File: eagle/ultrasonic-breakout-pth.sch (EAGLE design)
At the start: 25 parts, among them Q1 16 MHz, U1 ATMEGA328P_PDIP

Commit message: improve board layout
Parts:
- C3: device SparkFun-Passives:CAPPTH1 -> SparkFun-Capacitors:CAPPTH
- Q1: device special:XTAL -> SparkFun-FreqCtrl:CRYSTALHC49UV
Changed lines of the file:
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@@
 <?xml version="1.0" encoding="utf-8"?>
 <!DOCTYPE eagle SYSTEM "eagle.dtd">
-<eagle version="7.5.0">
+<eagle version="7.1.0">
 <drawing>
 <settings>
@@
 <parts>
 <part name="U1" library="SparkFun-DigitalIC" deviceset="ATMEGA328P_PDIP" device=""/>
-<part name="Q1" library="special" deviceset="XTAL" device="" value="16 MHz"/>
+<part name="Q1" library="SparkFun-FreqCtrl" deviceset="CRYSTAL" device="HC49UV" value="16 MHz"/>
 <part name="C1" library="SparkFun-Passives" deviceset="CAP" device="PTH" value="2.2pF"/>
 <part name="C2" library="SparkFun-Passives" deviceset="CAP" device="PTH" value="2.2pF"/>
@@
 <part name="HCSR04-8" library="SparkFun-Connectors" deviceset="M04" device="PTH"/>
 <part name="R8" library="SparkFun-Passives" deviceset="RESISTOR" device="PTH-1/4W" value="2.2k"/>
-<part name="C3" library="SparkFun-Passives" deviceset="CAP" device="PTH1" value="0.1uF"/>
+<part name="C3" library="SparkFun-Capacitors" deviceset="CAP" device="PTH" value="0.1uF"/>
 <part name="R9" library="SparkFun-Passives" deviceset="RESISTOR" device="PTH-1/4W" value="330"/>
 <part name="D1" library="SparkFun-LED" deviceset="LED" device="5MM" value="GREEN"/>
@@
 <wire x1="2.54" y1="63.5" x2="7.62" y2="63.5" width="0.1524" layer="91"/>
 <pinref part="Q1" gate="G$1" pin="1"/>
-<wire x1="7.62" y1="63.5" x2="7.62" y2="60.96" width="0.1524" layer="91"/>
+<wire x1="7.62" y1="63.5" x2="7.62" y2="58.42" width="0.1524" layer="91"/>
 <pinref part="U1" gate="G$1" pin="PB6(XTAL1/TOSC1)"/>
 <wire x1="17.78" y1="58.42" x2="15.24" y2="58.42" width="0.1524" layer="91"/>
@@
 <wire x1="7.62" y1="48.26" x2="2.54" y2="48.26" width="0.1524" layer="91"/>
 <pinref part="Q1" gate="G$1" pin="2"/>
-<wire x1="7.62" y1="48.26" x2="7.62" y2="50.8" width="0.1524" layer="91"/>
+<wire x1="7.62" y1="48.26" x2="7.62" y2="53.34" width="0.1524" layer="91"/>
 </segment>
 </net>

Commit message: improve board layout
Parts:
- renumbered D1 to LED, HCSR04-1 to 1, HCSR04-2 to 2, HCSR04-3 to 3, HCSR04-4 to 4, HCSR04-5 to 5, HCSR04-6 to 6, HCSR04-7 to 7, HCSR04-8 to 8, JP1 to AVR
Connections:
- net N$4 renamed TRIGGER1

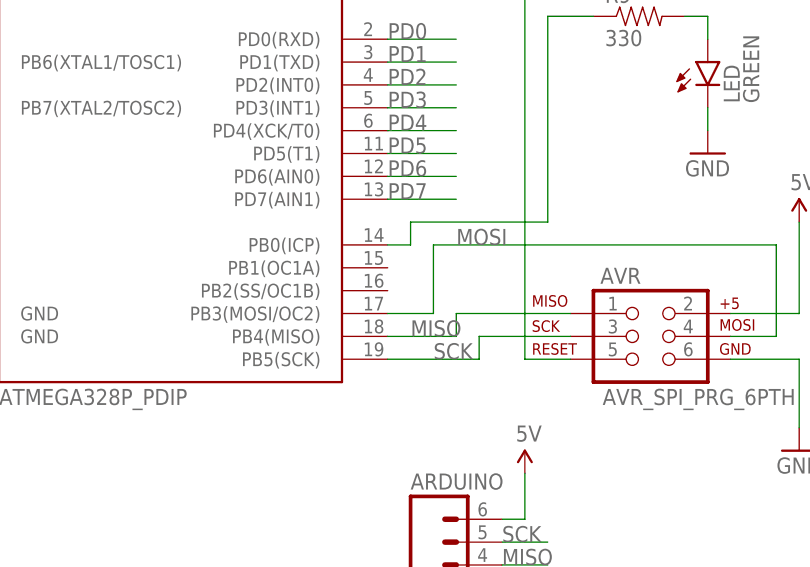
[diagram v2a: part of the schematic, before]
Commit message: fixed missing SS connection in schematic, also switched to 5mm capacitor and completely redesigned board layout
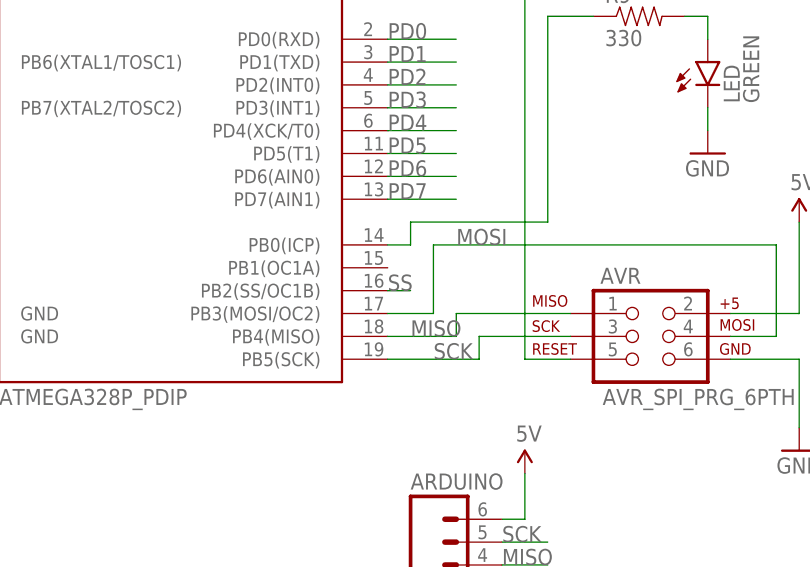
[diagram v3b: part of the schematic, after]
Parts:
- ARDUINO: device SparkFun-Connectors:M06RA -> SparkFun-Connectors:M06LOCK
- C3: device SparkFun-Capacitors:CAPPTH -> SparkFun-Capacitors:CAPPTH1
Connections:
- net SS: now also U1.PB2(SS/OC1B)
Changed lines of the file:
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@@
 <part name="SUPPLY2" library="SparkFun-Aesthetics" deviceset="5V" device=""/>
 <part name="GND3" library="SparkFun-Aesthetics" deviceset="GND" device=""/>
-<part name="ARDUINO" library="SparkFun-Connectors" deviceset="M06" device="RA"/>
+<part name="ARDUINO" library="SparkFun-Connectors" deviceset="M06" device="LOCK"/>
 <part name="SUPPLY3" library="SparkFun-Aesthetics" deviceset="5V" device=""/>
 <part name="GND4" library="SparkFun-Aesthetics" deviceset="GND" device=""/>
@@
 <part name="8" library="SparkFun-Connectors" deviceset="M04" device="PTH"/>
 <part name="R8" library="SparkFun-Passives" deviceset="RESISTOR" device="PTH-1/4W" value="2.2k"/>
-<part name="C3" library="SparkFun-Capacitors" deviceset="CAP" device="PTH" value="0.1uF"/>
+<part name="C3" library="SparkFun-Capacitors" deviceset="CAP" device="PTH1" value="0.1uF"/>
 <part name="R9" library="SparkFun-Passives" deviceset="RESISTOR" device="PTH-1/4W" value="330"/>
 <part name="LED" library="SparkFun-LED" deviceset="LED" device="5MM" value="GREEN"/>
@@
 <label x="78.74" y="-2.54" size="1.778" layer="95"/>
 </segment>
-</net>
+<segment>
+<pinref part="U1" gate="G$1" pin="PB2(SS/OC1B)"/>
+<wire x1="66.04" y1="33.02" x2="68.58" y2="33.02" width="0.1524" layer="91"/>
+<label x="66.04" y="33.02" size="1.778" layer="95"/>
+</segment>
+</net>

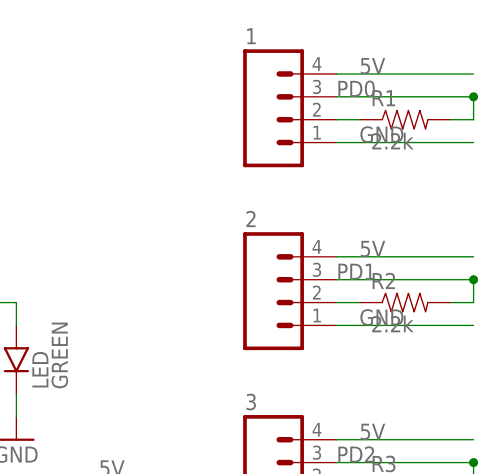
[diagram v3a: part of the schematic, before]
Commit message: changed first connecter to swap trig/echo
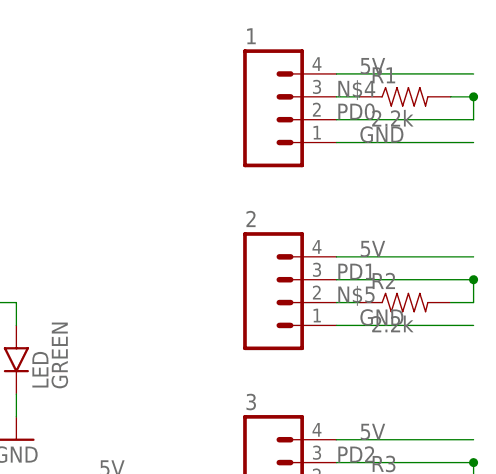
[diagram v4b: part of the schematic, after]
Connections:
- removed net TRIGGER1: 1.2, R1.1
- new net N$4: 1.3, R1.1
- net PD0: now also 1.2; no longer 1.3
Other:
- moved on the sheet: R1
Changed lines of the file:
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@@
 <instance part="GND4" gate="1" x="81.28" y="-12.7"/>
 <instance part="1" gate="G$1" x="132.08" y="83.82"/>
-<instance part="R1" gate="G$1" x="144.78" y="83.82"/>
+<instance part="R1" gate="G$1" x="144.78" y="86.36"/>
 <instance part="2" gate="G$1" x="132.08" y="63.5"/>
 <instance part="R2" gate="G$1" x="144.78" y="63.5"/>
@@
 </segment>
 </net>
-<net name="TRIGGER1" class="0">
-<segment>
-<pinref part="1" gate="G$1" pin="2"/>
-<pinref part="R1" gate="G$1" pin="1"/>
-<wire x1="137.16" y1="83.82" x2="139.7" y2="83.82" width="0.1524" layer="91"/>
-</segment>
-</net>
 <net name="PD0" class="0">
-<segment>
-<pinref part="1" gate="G$1" pin="3"/>
-<wire x1="137.16" y1="86.36" x2="152.4" y2="86.36" width="0.1524" layer="91"/>
-<junction x="152.4" y="86.36"/>
-<wire x1="152.4" y1="86.36" x2="152.4" y2="83.82" width="0.1524" layer="91"/>
-<pinref part="R1" gate="G$1" pin="2"/>
-<wire x1="152.4" y1="83.82" x2="149.86" y2="83.82" width="0.1524" layer="91"/>
-<label x="137.16" y="86.36" size="1.778" layer="95"/>
-</segment>
 <segment>
 <pinref part="U1" gate="G$1" pin="PD0(RXD)"/>
 <wire x1="66.04" y1="60.96" x2="73.66" y2="60.96" width="0.1524" layer="91"/>
 <label x="66.04" y="60.96" size="1.778" layer="95"/>
+</segment>
+<segment>
+<pinref part="R1" gate="G$1" pin="2"/>
+<wire x1="149.86" y1="86.36" x2="152.4" y2="86.36" width="0.1524" layer="91"/>
+<junction x="152.4" y="86.36"/>
+<wire x1="152.4" y1="86.36" x2="152.4" y2="83.82" width="0.1524" layer="91"/>
+<pinref part="1" gate="G$1" pin="2"/>
+<wire x1="152.4" y1="83.82" x2="137.16" y2="83.82" width="0.1524" layer="91"/>
+<label x="137.16" y="83.82" size="1.778" layer="95"/>
 </segment>
 </net>
@@
 <pinref part="R2" gate="G$1" pin="1"/>
 <wire x1="137.16" y1="63.5" x2="139.7" y2="63.5" width="0.1524" layer="91"/>
+<label x="137.16" y="63.5" size="1.778" layer="95"/>
 </segment>
 </net>
@@
 </segment>
 </net>
+<net name="N$4" class="0">
+<segment>
+<pinref part="1" gate="G$1" pin="3"/>
+<pinref part="R1" gate="G$1" pin="1"/>
+<wire x1="137.16" y1="86.36" x2="139.7" y2="86.36" width="0.1524" layer="91"/>
+<label x="137.16" y="86.36" size="1.778" layer="95"/>
+</segment>
+</net>

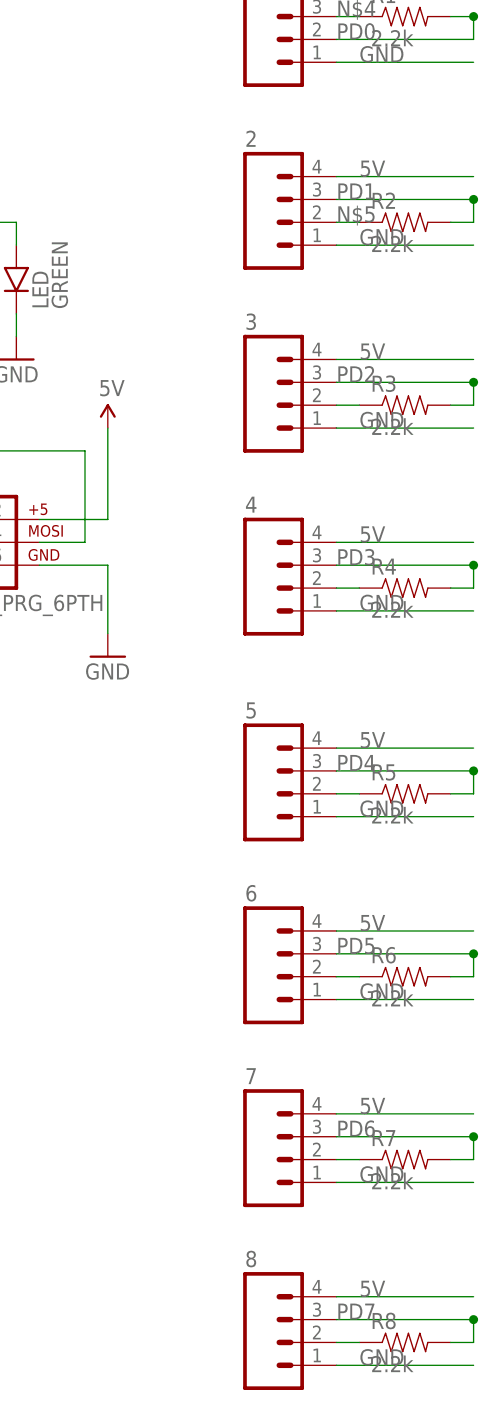
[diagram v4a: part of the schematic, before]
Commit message: finished swapping trig/echo on all connectors
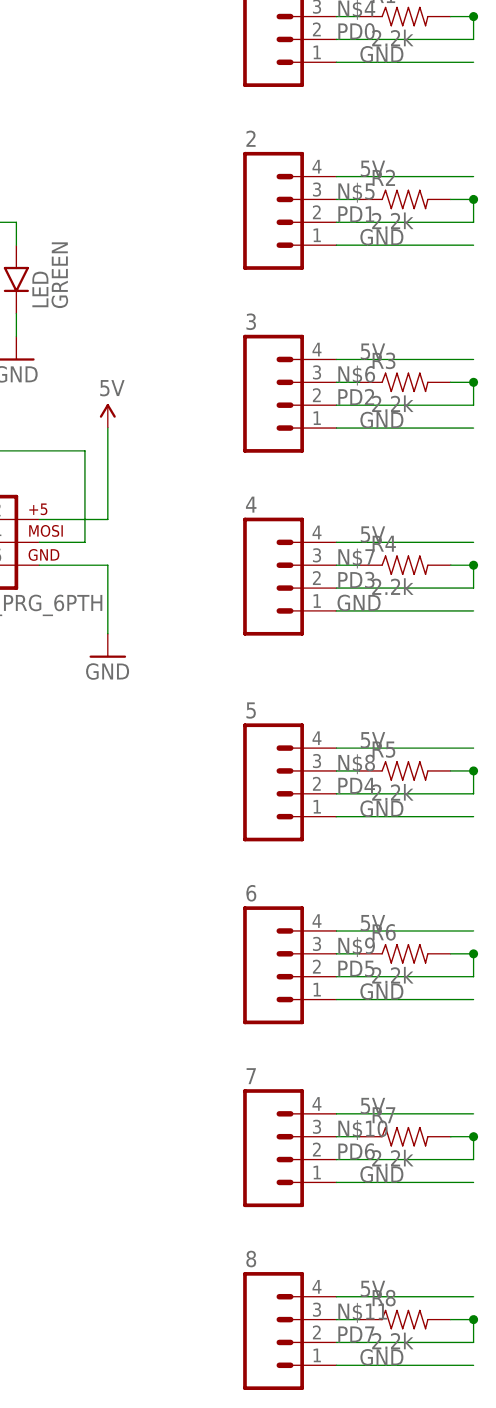
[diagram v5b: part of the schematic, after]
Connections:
- net N$10: now also 7.3; no longer 7.2
- net N$11: now also 8.3; no longer 8.2
- net N$5: now also 2.3; no longer 2.2
- net N$6: now also 3.3; no longer 3.2
- net N$7: now also 4.3; no longer 4.2
- net N$8: now also 5.3; no longer 5.2
- net N$9: now also 6.3; no longer 6.2
- net PD1: now also 2.2; no longer 2.3
- net PD2: now also 3.2; no longer 3.3
- net PD3: now also 4.2; no longer 4.3
- net PD4: now also 5.2; no longer 5.3
- net PD5: now also 6.2; no longer 6.3
- net PD6: now also 7.2; no longer 7.3
- net PD7: now also 8.2; no longer 8.3
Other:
- moved on the sheet: R2, R3, R4, R5, R6, R7, R8

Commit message: update board to use locking molex connectors
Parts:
- 1, 2, 3, 4, 5, 6, 7, 8: device SparkFun-Connectors:M04PTH -> SparkFun-Connectors:M04LOCK
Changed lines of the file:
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@@
 <?xml version="1.0" encoding="utf-8"?>
 <!DOCTYPE eagle SYSTEM "eagle.dtd">
-<eagle version="7.1.0">
+<eagle version="7.5.0">
 <drawing>
 <settings>
@@
 <part name="SUPPLY3" library="SparkFun-Aesthetics" deviceset="5V" device=""/>
 <part name="GND4" library="SparkFun-Aesthetics" deviceset="GND" device=""/>
-<part name="1" library="SparkFun-Connectors" deviceset="M04" device="PTH"/>
+<part name="1" library="SparkFun-Connectors" deviceset="M04" device="LOCK"/>
 <part name="R1" library="SparkFun-Passives" deviceset="RESISTOR" device="PTH-1/4W" value="2.2k"/>
-<part name="2" library="SparkFun-Connectors" deviceset="M04" device="PTH"/>
+<part name="2" library="SparkFun-Connectors" deviceset="M04" device="LOCK"/>
 <part name="R2" library="SparkFun-Passives" deviceset="RESISTOR" device="PTH-1/4W" value="2.2k"/>
-<part name="3" library="SparkFun-Connectors" deviceset="M04" device="PTH"/>
+<part name="3" library="SparkFun-Connectors" deviceset="M04" device="LOCK"/>
 <part name="R3" library="SparkFun-Passives" deviceset="RESISTOR" device="PTH-1/4W" value="2.2k"/>
-<part name="4" library="SparkFun-Connectors" deviceset="M04" device="PTH"/>
+<part name="4" library="SparkFun-Connectors" deviceset="M04" device="LOCK"/>
 <part name="R4" library="SparkFun-Passives" deviceset="RESISTOR" device="PTH-1/4W" value="2.2k"/>
-<part name="5" library="SparkFun-Connectors" deviceset="M04" device="PTH"/>
+<part name="5" library="SparkFun-Connectors" deviceset="M04" device="LOCK"/>
 <part name="R5" library="SparkFun-Passives" deviceset="RESISTOR" device="PTH-1/4W" value="2.2k"/>
-<part name="6" library="SparkFun-Connectors" deviceset="M04" device="PTH"/>
+<part name="6" library="SparkFun-Connectors" deviceset="M04" device="LOCK"/>
 <part name="R6" library="SparkFun-Passives" deviceset="RESISTOR" device="PTH-1/4W" value="2.2k"/>
-<part name="7" library="SparkFun-Connectors" deviceset="M04" device="PTH"/>
+<part name="7" library="SparkFun-Connectors" deviceset="M04" device="LOCK"/>
 <part name="R7" library="SparkFun-Passives" deviceset="RESISTOR" device="PTH-1/4W" value="2.2k"/>
-<part name="8" library="SparkFun-Connectors" deviceset="M04" device="PTH"/>
+<part name="8" library="SparkFun-Connectors" deviceset="M04" device="LOCK"/>
 <part name="R8" library="SparkFun-Passives" deviceset="RESISTOR" device="PTH-1/4W" value="2.2k"/>
 <part name="C3" library="SparkFun-Capacitors" deviceset="CAP" device="PTH1" value="0.1uF"/>
